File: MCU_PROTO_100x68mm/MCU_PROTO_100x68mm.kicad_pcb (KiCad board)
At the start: 2 copper layers, 90 x 58 mm, 333 parts, among them J1 Screw_Terminal_01x04, J10 Conn_01x20_Female, J11 Conn_01x01_Male, J12 Conn_01x01_Male, J2 Screw_Terminal_01x04, J3 Conn_01x20_Female, J4 Conn_01x20_Female, J5 Conn_01x20_Female, J6 Conn_01x20_Female, J7 Conn_01x20_Female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

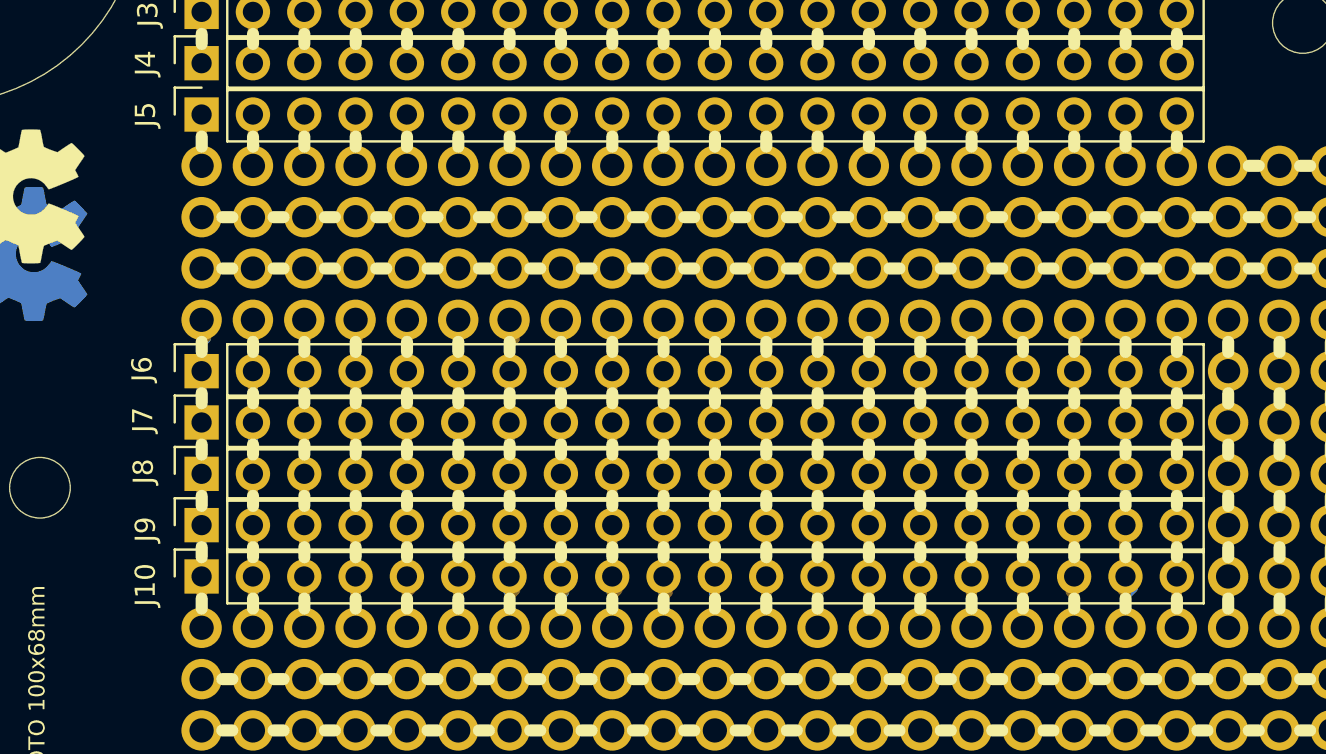
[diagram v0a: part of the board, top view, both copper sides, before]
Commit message: improved connector place
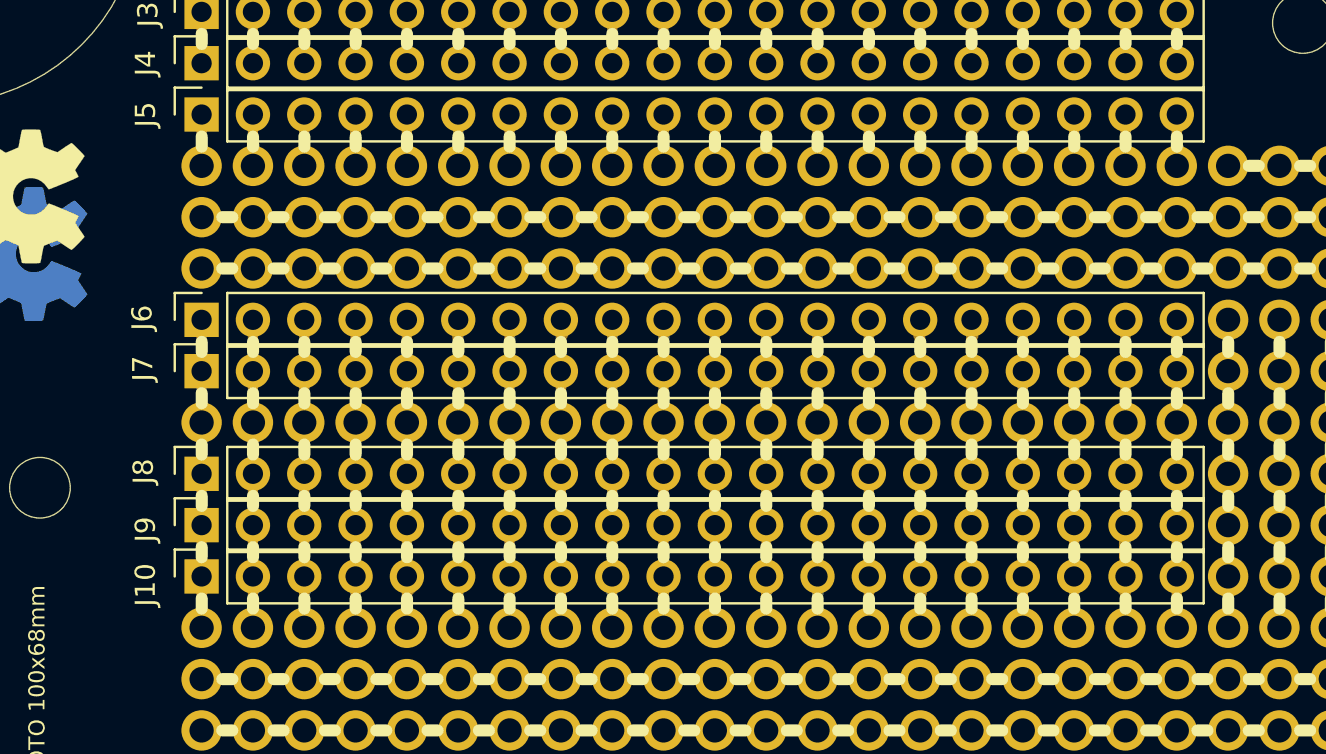
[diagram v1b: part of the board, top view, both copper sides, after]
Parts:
- removed the REF** at (161.3, 120.7)
- removed the REF** at (158.7, 120.7)
- removed the REF** at (156.2, 120.7)
- removed the REF** at (153.6, 120.7)
- removed the REF** at (151.1, 120.7)
- removed the REF** at (148.6, 120.7)
- removed the REF** at (146.0, 120.7)
- removed the REF** at (143.5, 120.7)
- removed the REF** at (140.9, 120.7)
- removed the REF** at (138.4, 120.7)
- removed the REF** at (135.9, 120.7)
- removed the REF** at (133.3, 120.7)
- removed the REF** at (130.8, 120.7)
- removed the REF** at (128.2, 120.7)
- removed the REF** at (125.7, 120.7)
- removed the REF** at (123.2, 120.7)
- removed the REF** at (120.6, 120.7)
- removed the REF** at (118.1, 120.7)
- removed the REF** at (115.5, 120.7)
- removed the REF** at (113.0, 120.7)
- added REF**: SolderWirePad_1x01_Drill0.8mm, Connector_Wire:SolderWirePad_1x01_Drill0.8mm, F.Cu at (140.9, 125.8)
- added REF**: SolderWirePad_1x01_Drill0.8mm, Connector_Wire:SolderWirePad_1x01_Drill0.8mm, F.Cu at (138.4, 125.8)
- added REF**: SolderWirePad_1x01_Drill0.8mm, Connector_Wire:SolderWirePad_1x01_Drill0.8mm, F.Cu at (135.9, 125.8)
- added REF**: SolderWirePad_1x01_Drill0.8mm, Connector_Wire:SolderWirePad_1x01_Drill0.8mm, F.Cu at (133.3, 125.8)
- added REF**: SolderWirePad_1x01_Drill0.8mm, Connector_Wire:SolderWirePad_1x01_Drill0.8mm, F.Cu at (130.8, 125.8)
- added REF**: SolderWirePad_1x01_Drill0.8mm, Connector_Wire:SolderWirePad_1x01_Drill0.8mm, F.Cu at (128.2, 125.8)
- added REF**: SolderWirePad_1x01_Drill0.8mm, Connector_Wire:SolderWirePad_1x01_Drill0.8mm, F.Cu at (125.7, 125.8)
- added REF**: SolderWirePad_1x01_Drill0.8mm, Connector_Wire:SolderWirePad_1x01_Drill0.8mm, F.Cu at (123.2, 125.8)
- added REF**: SolderWirePad_1x01_Drill0.8mm, Connector_Wire:SolderWirePad_1x01_Drill0.8mm, F.Cu at (120.6, 125.8)
- added REF**: SolderWirePad_1x01_Drill0.8mm, Connector_Wire:SolderWirePad_1x01_Drill0.8mm, F.Cu at (118.1, 125.8)
- added REF**: SolderWirePad_1x01_Drill0.8mm, Connector_Wire:SolderWirePad_1x01_Drill0.8mm, F.Cu at (161.3, 125.8)
- added REF**: SolderWirePad_1x01_Drill0.8mm, Connector_Wire:SolderWirePad_1x01_Drill0.8mm, F.Cu at (115.5, 125.8)
- added REF**: SolderWirePad_1x01_Drill0.8mm, Connector_Wire:SolderWirePad_1x01_Drill0.8mm, F.Cu at (113.0, 125.8)
- added REF**: SolderWirePad_1x01_Drill0.8mm, Connector_Wire:SolderWirePad_1x01_Drill0.8mm, F.Cu at (158.7, 125.8)
- added REF**: SolderWirePad_1x01_Drill0.8mm, Connector_Wire:SolderWirePad_1x01_Drill0.8mm, F.Cu at (156.2, 125.8)
- added REF**: SolderWirePad_1x01_Drill0.8mm, Connector_Wire:SolderWirePad_1x01_Drill0.8mm, F.Cu at (153.6, 125.8)
- added REF**: SolderWirePad_1x01_Drill0.8mm, Connector_Wire:SolderWirePad_1x01_Drill0.8mm, F.Cu at (151.1, 125.8)
- added REF**: SolderWirePad_1x01_Drill0.8mm, Connector_Wire:SolderWirePad_1x01_Drill0.8mm, F.Cu at (148.6, 125.8)
- added REF**: SolderWirePad_1x01_Drill0.8mm, Connector_Wire:SolderWirePad_1x01_Drill0.8mm, F.Cu at (146.0, 125.8)
- added REF**: SolderWirePad_1x01_Drill0.8mm, Connector_Wire:SolderWirePad_1x01_Drill0.8mm, F.Cu at (143.5, 125.8)
- moved J6 2.54 mm to (113.0, 120.7)
- moved J7 2.54 mm to (113.0, 123.2)
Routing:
- net Net-(J7-Pad11): track 3.31 -> 7.57 mm
- net Net-(J7-Pad17): track 3.27 -> 7.13 mm
- net Net-(J7-Pad20): track 3.33 -> 7.16 mm
- net Net-(J7-Pad1): track 3.28 -> 7.08 mm
- net Net-(J7-Pad19): track 3.56 -> 7.35 mm
- net Net-(J7-Pad18): track 3.23 -> 7.02 mm
- net Net-(J7-Pad7): track 3.42 -> 7.18 mm
- net Net-(J6-Pad1): track 3.61 -> 0.12 mm
- net Net-(J7-Pad13): track 3.42 -> 6.89 mm
- net Net-(J7-Pad4): track 3.45 -> 6.89 mm
- net Net-(J6-Pad7): track 3.34 -> 0.00 mm
- net Net-(J6-Pad19): track 3.33 -> 0.00 mm
- net Net-(J6-Pad4): track 3.32 -> 0.00 mm
- net Net-(J6-Pad20): track 3.22 -> 0.00 mm
- net Net-(J6-Pad18): track 3.21 -> 0.00 mm
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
